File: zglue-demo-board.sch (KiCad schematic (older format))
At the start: 142 parts, among them J1 3220-10-0100-00, J10 0473460001, J2 DF13A-2P-1.25H, J3 3220-10-0100-00, J4 2x20_Header_Female, J5 0473460001, J6 556500488, J7 556500488, J8 WE_686115148922, J9 WE_686115148922_FLIPPED, U1 MCP1700T-3302E_TT, U2 NTS0104BQ, U3 NTS0104BQ, U4 NTS0104BQ, U5 93LC56CT-IMC, U6 FT4232HQ, U7 NTB0104BQ, U8 NTB0104BQ, Y1 ASFLMB-12.000MHZ-LC-T

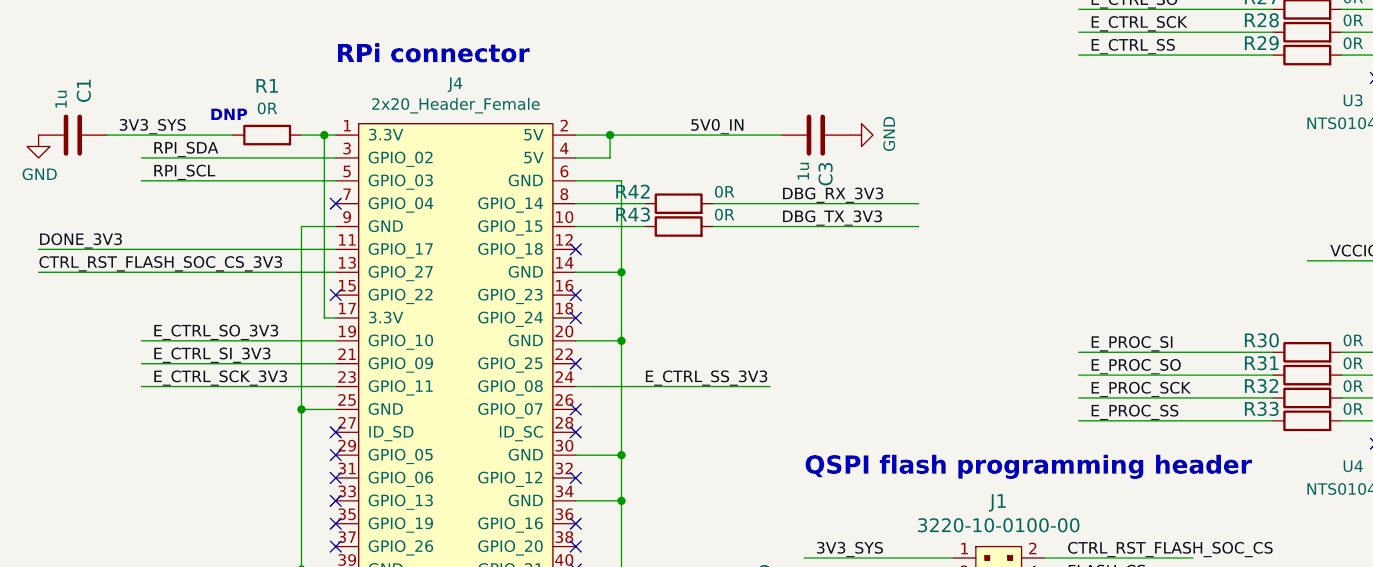
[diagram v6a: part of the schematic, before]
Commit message: Tied SPI signals for programming second FPGA from RPi
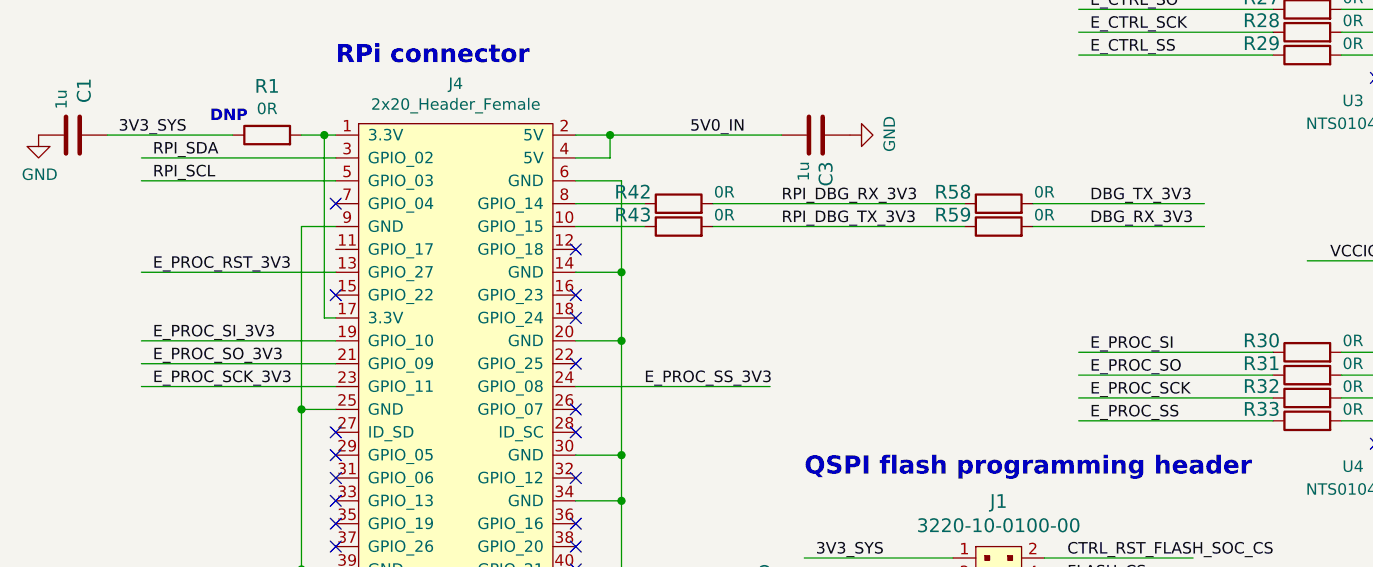
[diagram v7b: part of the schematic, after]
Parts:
- added R58, R59: R_0R_0402, antmicro-footprints:0402-res, symbol antmicroResistors0402:R_0R_0402
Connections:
- net labels added: RPI_DBG_RX_3V3, RPI_DBG_TX_3V3
- wire segments 521 -> 522
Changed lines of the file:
@@
 	3200 4250 2900 4250
 Wire Wire Line
-	3500 4150 4400 4150
-Wire Wire Line
-	3500 4250 4400 4250
+	3500 4150 4600 4150
+Wire Wire Line
+	3500 4250 4600 4250
 Text Label 3800 4150 0    50   ~ 0
-DBG_RX_3V3
+RPI_DBG_RX_3V3
 Text Label 3800 4250 0    50   ~ 0
-DBG_TX_3V3
+RPI_DBG_TX_3V3
 Wire Wire Line
 	1850 3950 1000 3950
@@
 DNP
 Wire Wire Line
-	1850 4450 550  4450
+	1850 4450 1000 4450
 Wire Wire Line
 	3750 4950 2900 4950
@@
 Wire Wire Line
 	1850 4950 1000 4950
-Wire Wire Line
-	1850 4350 550  4350
-Text Label 550  4350 0    50   ~ 0
-DONE_3V3
-Text Label 1050 4950 0    50   ~ 0
-E_CTRL_SCK_3V3
-Text Label 1050 4750 0    50   ~ 0
-E_CTRL_SO_3V3
-Text Label 1050 4850 0    50   ~ 0
-E_CTRL_SI_3V3
-Text Label 3200 4950 0    50   ~ 0
-E_CTRL_SS_3V3
-Text Label 550  4450 0    50   ~ 0
-CTRL_RST_FLASH_SOC_CS_3V3
 $Comp
 L antmicroRectangularConnectorsHeadersMalePins:3220-10-0100-00 J1
@@
 	1    0    0    -1
 $EndComp
+Text Label 1050 4450 0    50   ~ 0
+E_PROC_RST_3V3
+Text Label 1050 4950 0    50   ~ 0
+E_PROC_SCK_3V3
+Text Label 3200 4950 0    50   ~ 0
+E_PROC_SS_3V3
+Text Label 1050 4850 0    50   ~ 0
+E_PROC_SO_3V3
+Text Label 1050 4750 0    50   ~ 0
+E_PROC_SI_3V3
+$Comp
+L antmicroResistors0402:R_0R_0402 R58
+U 1 1 5DEF0282
+P 4750 4150
+F 0 "R58" H 4550 4200 60  0000 C CNN
+F 1 "R_0R_0402" H 4750 4000 60  0001 C CNN
+F 2 "antmicro-footprints:0402-res" H 4950 4350 60  0001 L CNN
+F 3 "" H 4750 4150 50  0001 C CNN
+F 4 "PANASONIC" H 4950 4550 60  0001 L CNN "Manufacturer"
+F 5 "ERJ2GE0R00X" H 4950 4450 60  0001 L CNN "MPN"
+F 6 "0R" H 4950 4200 50  0000 C CNN "Val"
+	1    4750 4150
+	1    0    0    -1
+$EndComp
+$Comp
+L antmicroResistors0402:R_0R_0402 R59
+U 1 1 5DEF05BB
+P 4750 4250
+F 0 "R59" H 4550 4300 60  0000 C CNN
+F 1 "R_0R_0402" H 4750 4100 60  0001 C CNN
+F 2 "antmicro-footprints:0402-res" H 4950 4450 60  0001 L CNN
+F 3 "" H 4750 4250 50  0001 C CNN
+F 4 "PANASONIC" H 4950 4650 60  0001 L CNN "Manufacturer"
+F 5 "ERJ2GE0R00X" H 4950 4550 60  0001 L CNN "MPN"
+F 6 "0R" H 4950 4300 50  0000 C CNN "Val"
+	1    4750 4250
+	1    0    0    -1
+$EndComp
+Wire Wire Line
+	4900 4150 5650 4150
+Wire Wire Line
+	4900 4250 5650 4250
+Text Label 5150 4250 0    50   ~ 0
+DBG_RX_3V3
+Text Label 5150 4150 0    50   ~ 0
+DBG_TX_3V3
 $EndSCHEMATC

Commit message: PCB cleanup, updated layout
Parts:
- added N2: zglue_logo, antmicro-footprints:zglue-logo, symbol antmicroMechanicalParts:zglue_logo
- added N3: oshw_logo, antmicro-footprints:oshw-logo, symbol antmicroMechanicalParts:oshw_logo
- JP1, JP2, JP3: symbol Jumper:Jumper_3_Open -> zglue-demo-board-rescue:Jumper_3_Open-Jumper
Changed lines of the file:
@@
 $EndComp
 $Comp
-L Jumper:Jumper_3_Open JP2
+L zglue-demo-board-rescue:Jumper_3_Open-Jumper JP2
 U 1 1 5F6F7935
 P 4350 2200
@@
 	4600 2500 3350 2500
 $Comp
-L Jumper:Jumper_3_Open JP3
+L zglue-demo-board-rescue:Jumper_3_Open-Jumper JP3
 U 1 1 5FF28200
 P 4350 2850
@@
 	4600 3150 3350 3150
 $Comp
-L Jumper:Jumper_3_Open JP1
+L zglue-demo-board-rescue:Jumper_3_Open-Jumper JP1
 U 1 1 5FF6DF38
 P 4350 1600
@@
 Text Label 5150 4150 0    50   ~ 0
 DBG_TX_3V3
+$Comp
+L antmicroMechanicalParts:oshw_logo N3
+U 1 1 5DE869F8
+P 8200 750
+F 0 "N3" H 8394 753 50  0000 L CNN
+F 1 "oshw_logo" H 8394 662 50  0000 L CNN
+F 2 "antmicro-footprints:oshw-logo" H 8220 510 50  0001 C CNN
+F 3 "" H 8200 750 50  0001 C CNN
+	1    8200 750
+	1    0    0    -1
+$EndComp
+$Comp
+L antmicroMechanicalParts:zglue_logo N2
+U 1 1 5DF9381C
+P 9000 750
+F 0 "N2" H 9194 753 50  0000 L CNN
+F 1 "zglue_logo" H 9194 662 50  0000 L CNN
+F 2 "antmicro-footprints:zglue-logo" H 9020 510 50  0001 C CNN
+F 3 "" H 9000 750 50  0001 C CNN
+	1    9000 750
+	1    0    0    -1
+$EndComp
 $EndSCHEMATC
